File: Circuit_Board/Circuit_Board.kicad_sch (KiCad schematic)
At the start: 41 parts, among them J1 Conn_01x02, J2 Control stuff, J3 Power stuff, J4 Conn_02x06_Odd_Even, J5 Conn_01x20_Socket, J6 Conn_01x20_Socket, J7 GPIO_1, J8 GPIO_2, J9 LED_AMP, Q2 IRF540N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

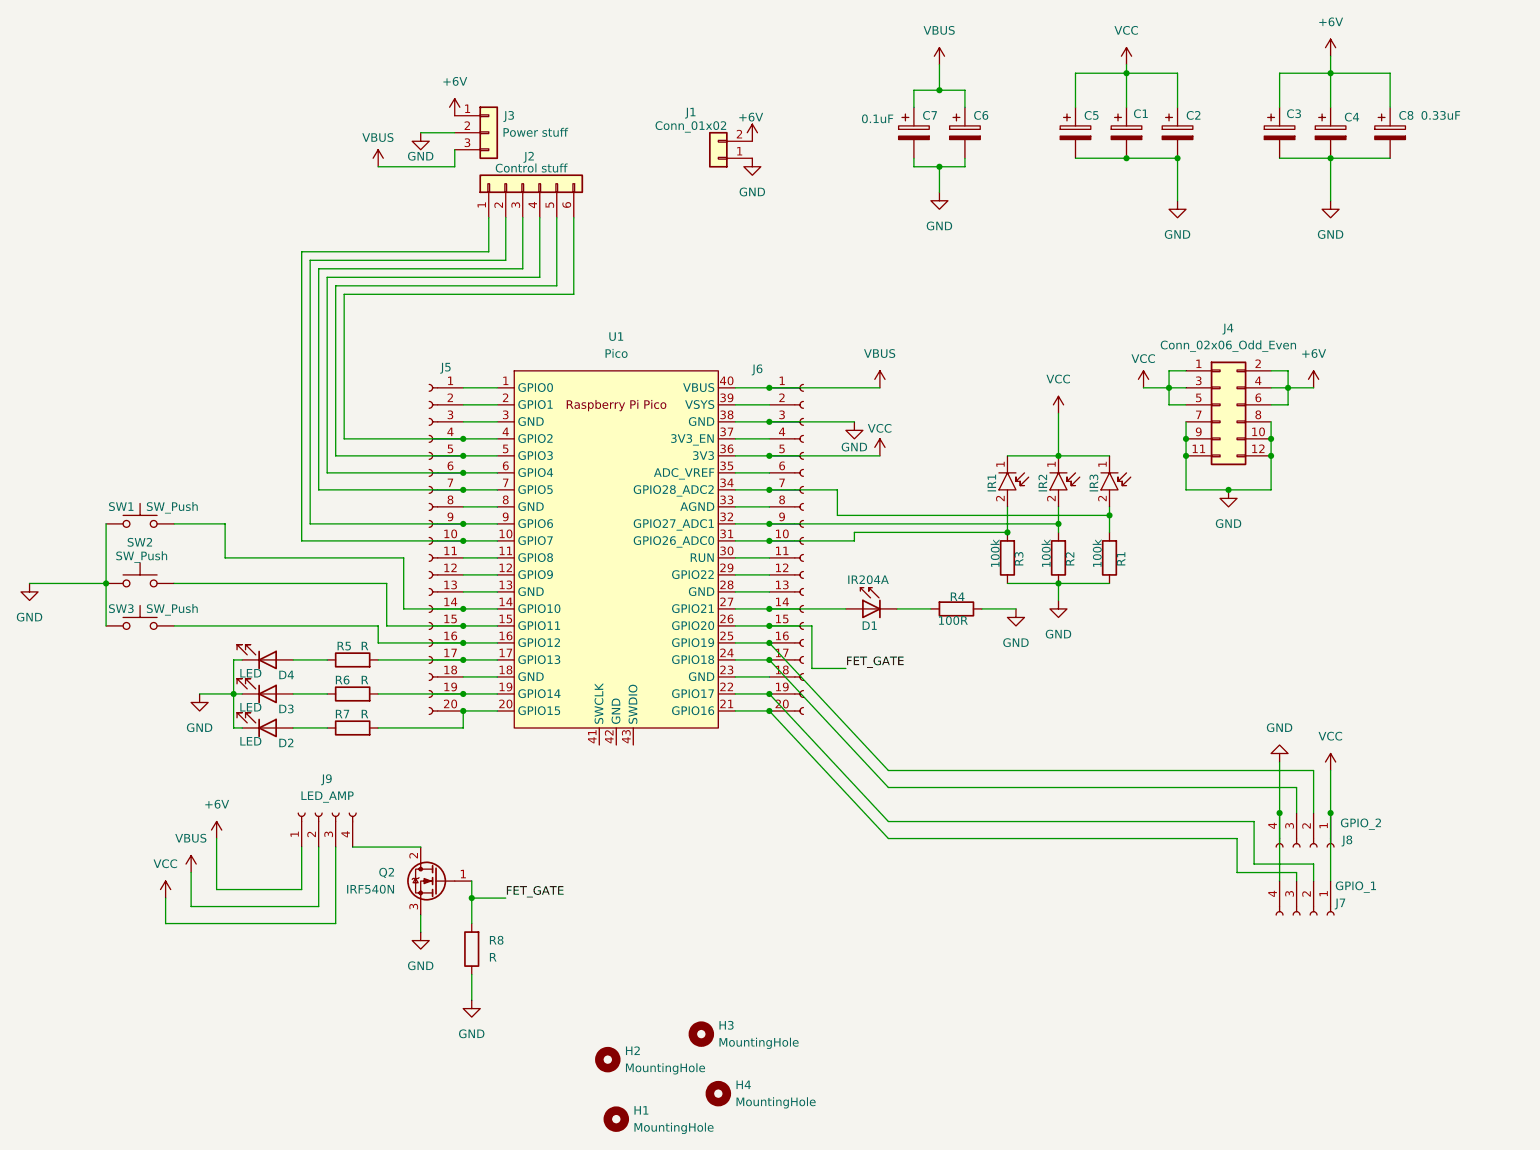
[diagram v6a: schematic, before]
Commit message: Updated component values
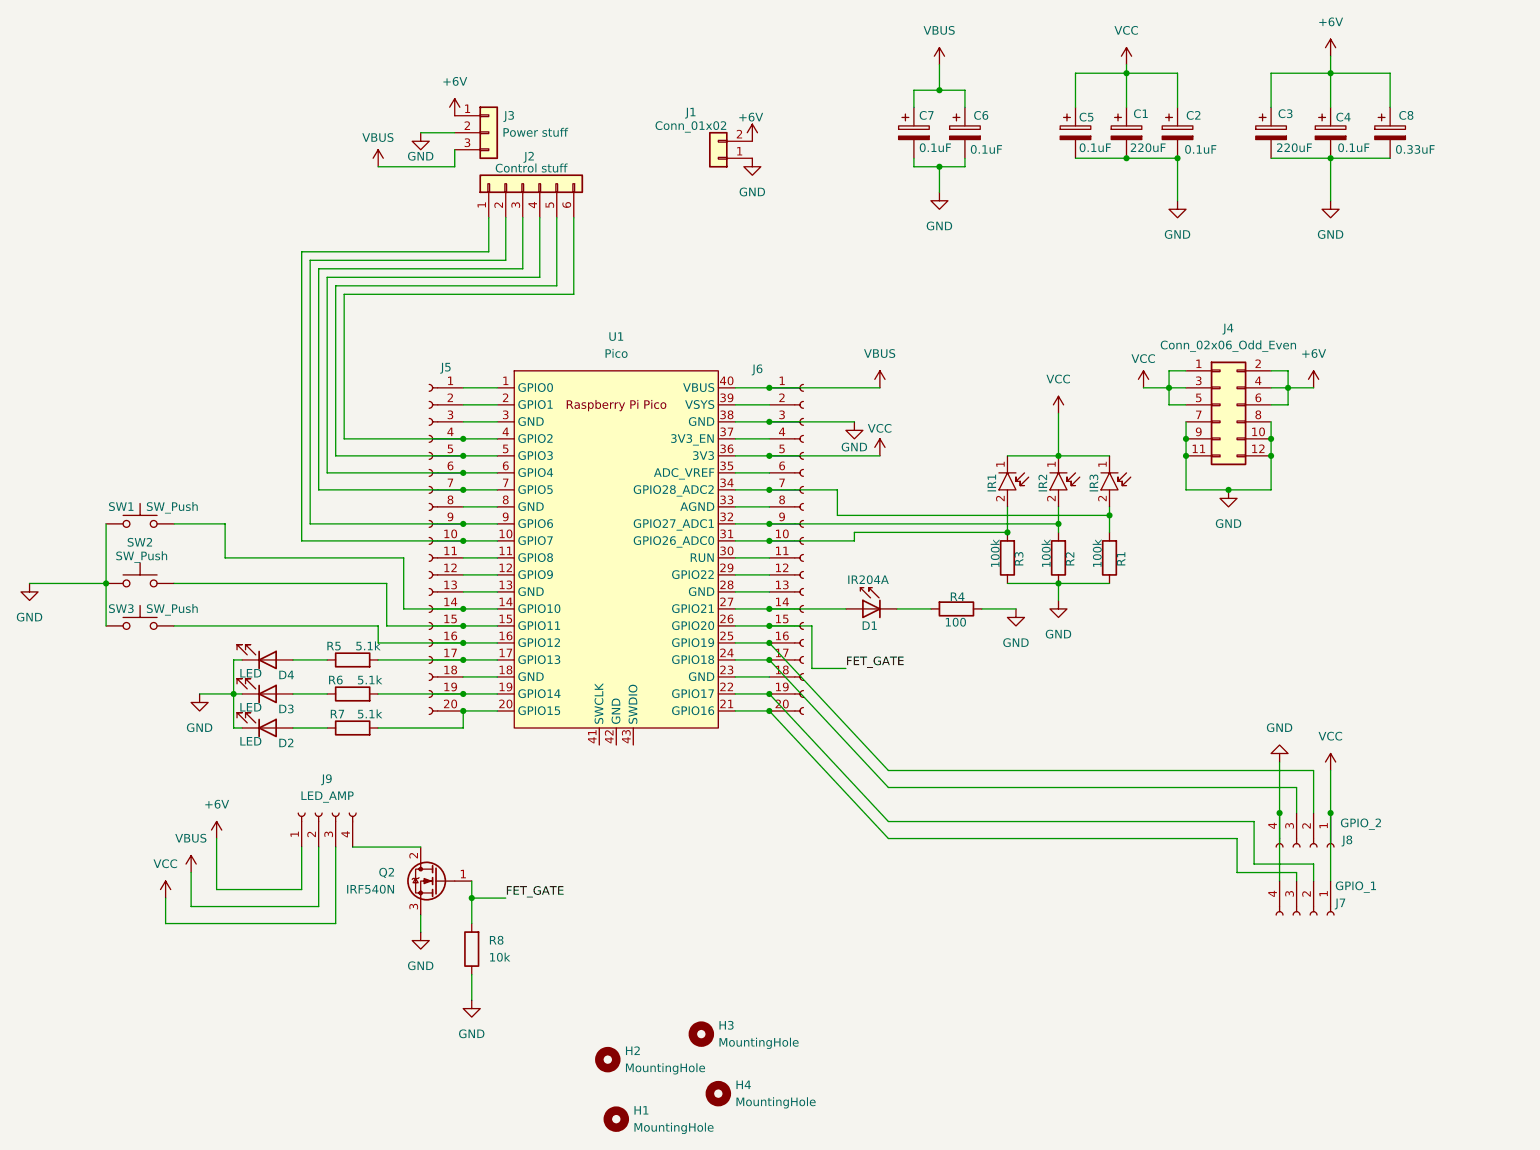
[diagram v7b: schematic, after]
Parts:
- C1, C3: value C_Polarized -> 220uF
- C2, C4, C5, C6: value C_Polarized -> 0.1uF
- R4: value 100R -> 100
- R5, R6, R7: value R -> 5.1k
- R8: value R -> 10k
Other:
- moved on the sheet: C3
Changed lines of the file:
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@@
 	)
 	(junction
-		(at 119.38 125.73)
-		(diameter 0)
-		(color 0 0 0 0)
-	)
-	(junction
 		(at 208.28 100.33)
 		(diameter 0)
@@
 	)
 	(junction
-		(at 218.44 45.72)
-		(diameter 0)
-		(color 0 0 0 0)
-	)
-	(junction
 		(at 227.33 90.17)
 		(diameter 0)
@@
 	)
 	(junction
+		(at 218.44 45.72)
+		(diameter 0)
+		(color 0 0 0 0)
+	)
+	(junction
 		(at 215.9 99.06)
 		(diameter 0)
@@
 	)
 	(junction
+		(at 119.38 125.73)
+		(diameter 0)
+		(color 0 0 0 0)
+	)
+	(junction
 		(at 119.38 118.11)
 		(diameter 0)
@@
 	(wire
 		(pts
-			(xy 241.3 38.1) (xy 241.3 33.02)
+			(xy 240.03 38.1) (xy 240.03 33.02)
 		)
 		(stroke
@@
 	(wire
 		(pts
-			(xy 241.3 33.02) (xy 248.92 33.02)
+			(xy 240.03 33.02) (xy 248.92 33.02)
 		)
 		(stroke
@@
 	(wire
 		(pts
-			(xy 241.3 45.72) (xy 248.92 45.72)
+			(xy 240.03 45.72) (xy 248.92 45.72)
 		)
 		(stroke
@@
 			)
 		)
-		(property "Value" "C_Polarized"
-			(at 198.12 42.2909 0)
-			(hide yes)
+		(property "Value" "0.1uF"
+			(at 195.072 44.45 0)
 			(show_name no)
 			(do_not_autoplace no)
@@
 		)
 		(property "Value" "0.33uF"
-			(at 262.382 39.37 0)
+			(at 258.572 44.45 0)
 			(show_name no)
 			(do_not_autoplace no)
@@
 			)
 		)
-		(property "Value" "C_Polarized"
-			(at 229.87 42.2909 0)
-			(hide yes)
+		(property "Value" "0.1uF"
+			(at 227.076 44.45 0)
 			(show_name no)
 			(do_not_autoplace no)
@@
 			)
 		)
-		(property "Value" "C_Polarized"
-			(at 204.978 41.91 0)
-			(hide yes)
+		(property "Value" "220uF"
+			(at 218.948 44.196 0)
 			(show_name no)
 			(do_not_autoplace no)
@@
 		(dnp no)
 		(property "Reference" "R7"
-			(at 101.346 128.778 90)
+			(at 100.584 128.778 90)
 			(show_name no)
 			(do_not_autoplace no)
@@
 			)
 		)
-		(property "Value" "R"
-			(at 104.648 128.778 90)
+		(property "Value" "5.1k"
+			(at 105.41 128.778 90)
 			(show_name no)
 			(do_not_autoplace no)
@@
 		(dnp no)
 		(property "Reference" "R6"
-			(at 101.346 123.698 90)
+			(at 100.33 123.698 90)
 			(show_name no)
 			(do_not_autoplace no)
@@
 			)
 		)
-		(property "Value" "R"
-			(at 104.648 123.698 90)
+		(property "Value" "5.1k"
+			(at 105.41 123.698 90)
 			(show_name no)
 			(do_not_autoplace no)
@@
 		(dnp no)
 		(property "Reference" "R5"
-			(at 101.6 118.618 90)
+			(at 100.076 118.618 90)
 			(show_name no)
 			(do_not_autoplace no)
@@
 			)
 		)
-		(property "Value" "R"
-			(at 104.648 118.618 90)
+		(property "Value" "5.1k"
+			(at 105.156 118.618 90)
 			(show_name no)
 			(do_not_autoplace no)
@@
 		(dnp no)
 		(property "Reference" "C7"
-			(at 187.96 39.37 0)
+			(at 187.452 39.37 0)
 			(show_name no)
 			(do_not_autoplace no)
@@
 		)
 		(property "Value" "0.1uF"
-			(at 178.816 39.878 0)
+			(at 187.452 44.196 0)
 			(show_name no)
 			(do_not_autoplace no)
@@
 			)
 		)
-		(property "Value" "100R"
-			(at 190.246 114.808 90)
+		(property "Value" "100"
+			(at 191.262 115.062 90)
 			(show_name no)
 			(do_not_autoplace no)
@@
 	(symbol
 		(lib_id "Device:C_Polarized")
-		(at 241.3 41.91 0)
+		(at 240.03 41.91 0)
 		(unit 1)
 		(body_style 1)
@@
 		(dnp no)
 		(property "Reference" "C3"
-			(at 242.316 39.116 0)
+			(at 241.046 39.116 0)
 			(show_name no)
 			(do_not_autoplace no)
@@
 			)
 		)
-		(property "Value" "C_Polarized"
-			(at 227.838 41.91 0)
-			(hide yes)
+		(property "Value" "220uF"
+			(at 240.792 44.196 0)
 			(show_name no)
 			(do_not_autoplace no)
@@
 		)
 		(property "Footprint" "Capacitor_THT:CP_Radial_D10.0mm_P5.00mm"
-			(at 242.2652 45.72 0)
+			(at 240.9952 45.72 0)
 			(hide yes)
 			(show_name no)
@@
 		)
 		(property "Datasheet" ""
-			(at 241.3 41.91 0)
+			(at 240.03 41.91 0)
 			(hide yes)
 			(show_name no)
@@
 		)
 		(property "Description" "Polarized capacitor"
-			(at 241.3 41.91 0)
+			(at 240.03 41.91 0)
 			(hide yes)
 			(show_name no)
@@
 			)
 		)
-		(property "Value" "R"
+		(property "Value" "10k"
 			(at 123.19 165.0999 0)
 			(show_name no)
@@
 		(dnp no)
 		(property "Reference" "C5"
-			(at 212.09 39.37 0)
+			(at 211.328 39.624 0)
 			(show_name no)
 			(do_not_autoplace no)
@@
 			)
 		)
-		(property "Value" "C_Polarized"
-			(at 214.63 42.2909 0)
-			(hide yes)
+		(property "Value" "0.1uF"
+			(at 211.328 44.196 0)
 			(show_name no)
 			(do_not_autoplace no)
@@
 		(dnp no)
 		(property "Reference" "C4"
-			(at 250.952 39.624 0)
+			(at 249.682 39.624 0)
 			(show_name no)
 			(do_not_autoplace no)
@@
 			)
 		)
-		(property "Value" "C_Polarized"
-			(at 252.73 42.2909 0)
-			(hide yes)
+		(property "Value" "0.1uF"
+			(at 249.936 44.196 0)
 			(show_name no)
 			(do_not_autoplace no)

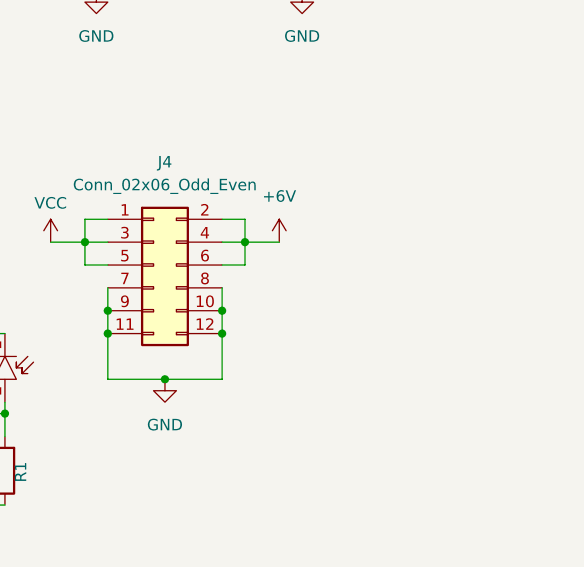
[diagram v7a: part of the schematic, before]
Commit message: Add 5+ receiver front panel model, update todo note on kicad file
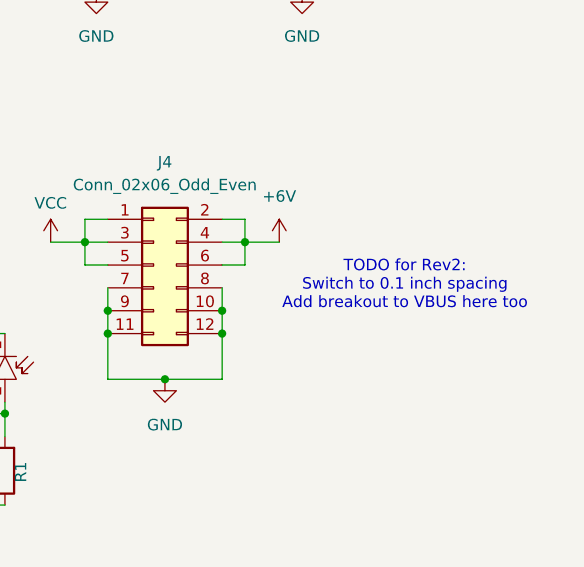
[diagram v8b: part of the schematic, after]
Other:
- note added: "TODO for Rev2: Switch to 0.1 inch spacing Add breakout to VBUS here too"
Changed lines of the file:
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@@
 	(generator_version "10.0")
 	(paper "A4")
+	(text "TODO for Rev2: \nSwitch to 0.1 inch spacing\nAdd breakout to VBUS here too"
+		(exclude_from_sim no)
+		(at 260.35 84.836 0)
+		(effects
+			(font
+				(size 1.27 1.27)
+			)
+		)
+	)
 	(junction
 		(at 218.44 33.02)
